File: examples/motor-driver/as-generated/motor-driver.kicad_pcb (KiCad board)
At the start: 2 copper layers, 100 x 50 mm, 12 parts, among them J1 VM 2.7-10.8V, J2 MOTOR A, J3 MOTOR B, J4 LOGIC, U1 DRV8833PW

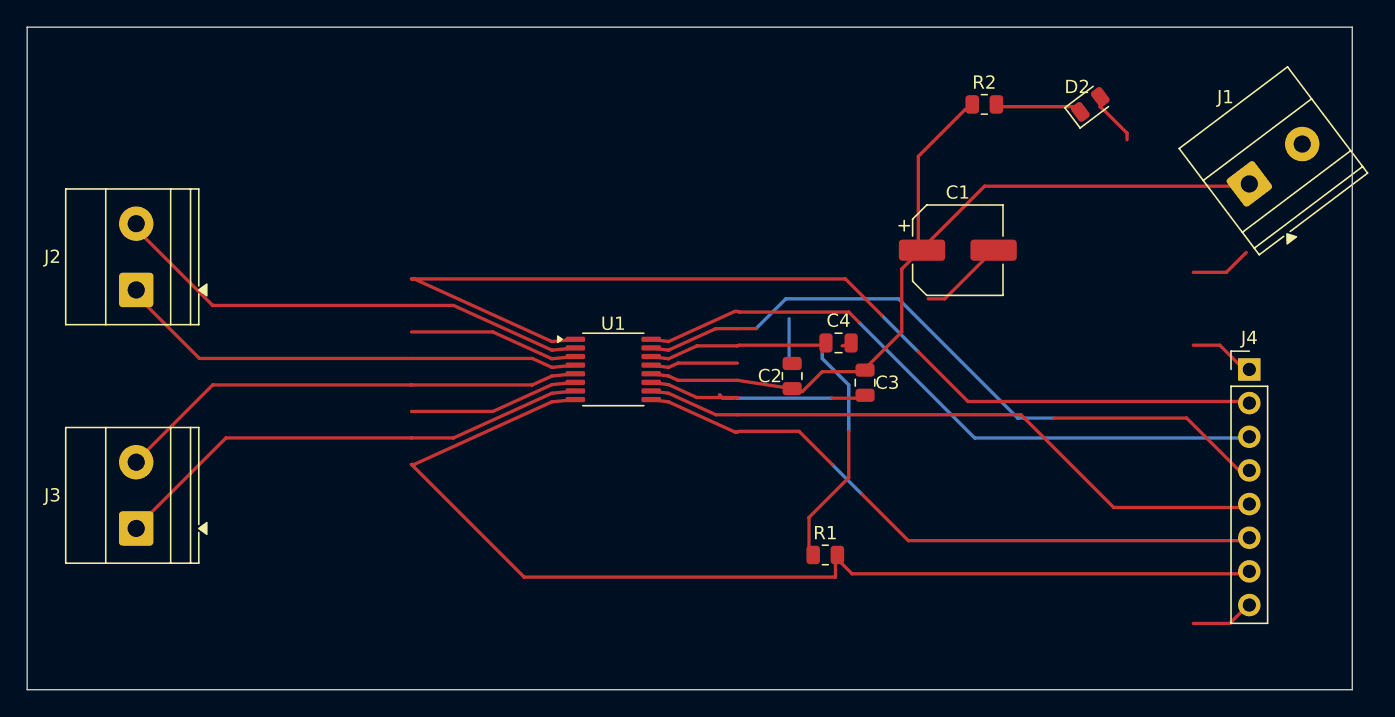
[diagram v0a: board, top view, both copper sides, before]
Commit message: Regenerate the five as round three drew them
All five reviewed projects pass their gates again: the buck all wire
with its feedback drawn home, the motor's logic named at the header,
the carrier reading as the pinout table it is - with its feed diode
finally pointing the right way - the filter compact with test points,
and the FPGA's capacitors sitting beside the units they feed. Thirty
renders redrawn, verdict tables at today's numbers.

Co-Authored-By: Claude Fable 5 <noreply@anthropic.com>
Claude-Session: https://claude.ai/code/session_01DUj7Ltu92tWg159mCSacwY
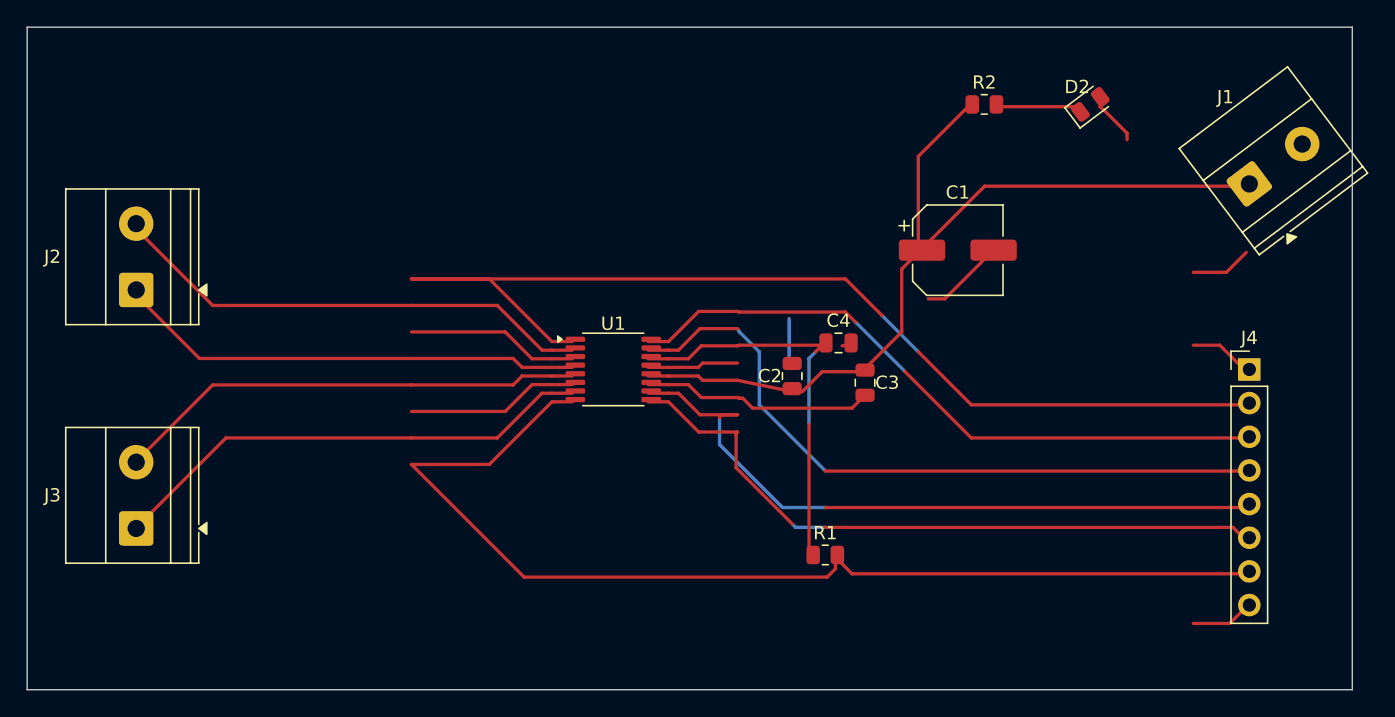
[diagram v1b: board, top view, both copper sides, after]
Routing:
- net /BIN2: track 48.2 -> 52.7 mm
- net /BIN1: track 48.8 -> 51.1 mm
- net /VCP: track 19.0 -> 17.2 mm
- net /VINT: track 31.3 -> 30.1 mm
- net /AIN2: track 51.6 -> 52.7 mm
- net /nSLEEP: track 80.4 -> 81.0 mm
- net /AIN1: track 49.4 -> 50.0 mm
- net GND: track 59.7 -> 60.3 mm

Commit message: Regenerate the four boards round four has settled
The buck, the motor driver, the carrier and the filter as the current
generator draws them: interior ground stitching on all four, the motor
driver's bundle tight and its board twelve millimetres shorter, the
filter compact and hand-placed, the carrier's indicator in a column of
its own. All four pass their gates. The FPGA is still regenerating.

Co-Authored-By: Claude Fable 5 <noreply@anthropic.com>
Claude-Session: https://claude.ai/code/session_01DUj7Ltu92tWg159mCSacwY
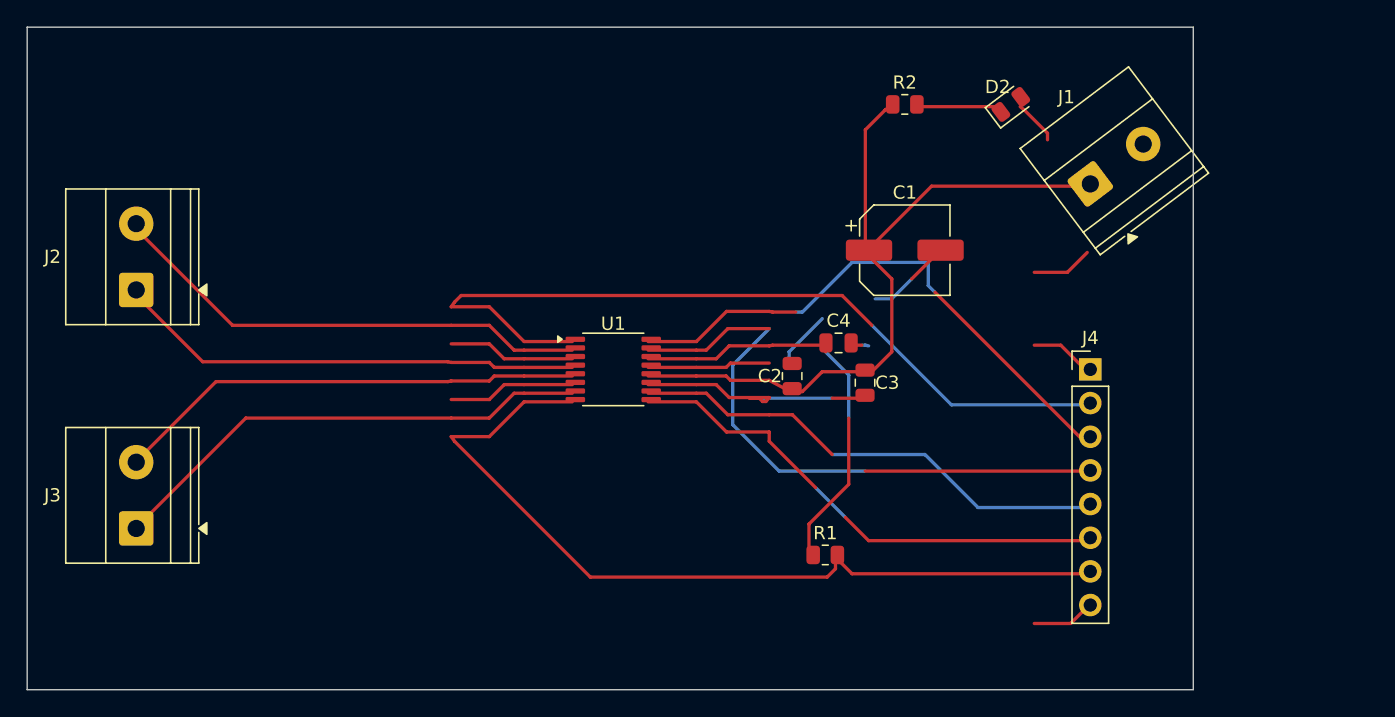
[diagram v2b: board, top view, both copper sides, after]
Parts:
- moved J1 12.0 mm to (180.2, 71.8)
- moved J4 12.0 mm to (180.2, 85.8)
- moved D2 6.00 mm to (174.2, 65.8)
- moved R2 6.00 mm to (166.2, 65.8)
- moved C1 4.00 mm to (166.2, 76.8)
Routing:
- net /nSLEEP: track 81.0 -> 62.0 mm
- net /nFAULT: track 82.3 -> 64.4 mm
- net /BIN2: track 52.7 -> 36.7 mm
- net /BIN1: track 51.1 -> 37.9 mm
- net /VM: track 67.2 -> 58.9 mm
- net /AIN1: track 50.0 -> 42.2 mm
- net /AIN2: track 52.7 -> 46.4 mm
- net /VCP: track 17.2 -> 19.8 mm
- net GND: track 60.3 -> 58.1 mm
- net /VINT: track 30.1 -> 31.7 mm
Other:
- board size 100 x 50 mm -> 88 x 50 mm

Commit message: Regenerate the four boards whose corners were off the grid
Ninety-one bends at angles nobody chose, now none. All four still pass
their gates.

Co-Authored-By: Claude Fable 5 <noreply@anthropic.com>
Claude-Session: https://claude.ai/code/session_01DUj7Ltu92tWg159mCSacwY
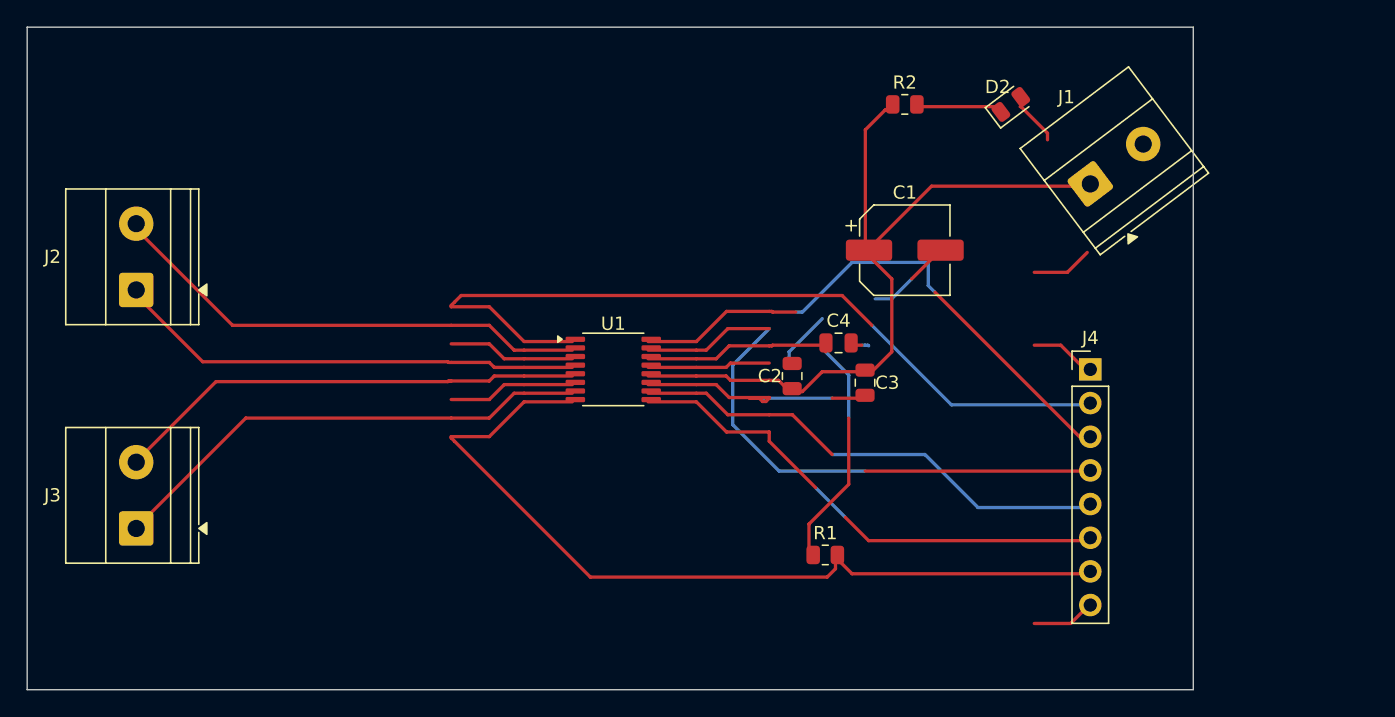
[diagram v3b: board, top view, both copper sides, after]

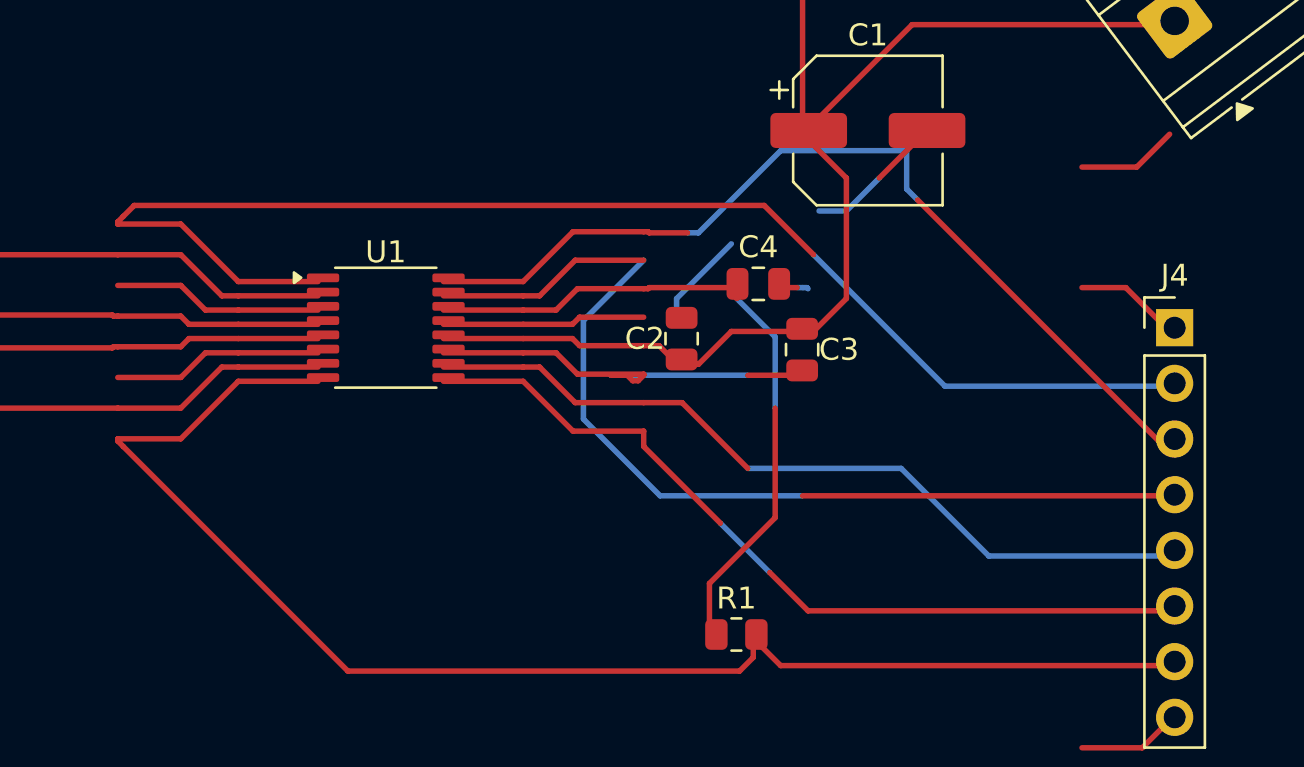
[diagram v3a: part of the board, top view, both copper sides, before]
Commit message: Regenerate the four the text and width work changed
Designators and values off the rails they were printed on, power-named
nets at the width their rule asks for, and the buck's feedback ending
on the capacitor pad it senses at.

Co-Authored-By: Claude Fable 5 <noreply@anthropic.com>
Claude-Session: https://claude.ai/code/session_01DUj7Ltu92tWg159mCSacwY
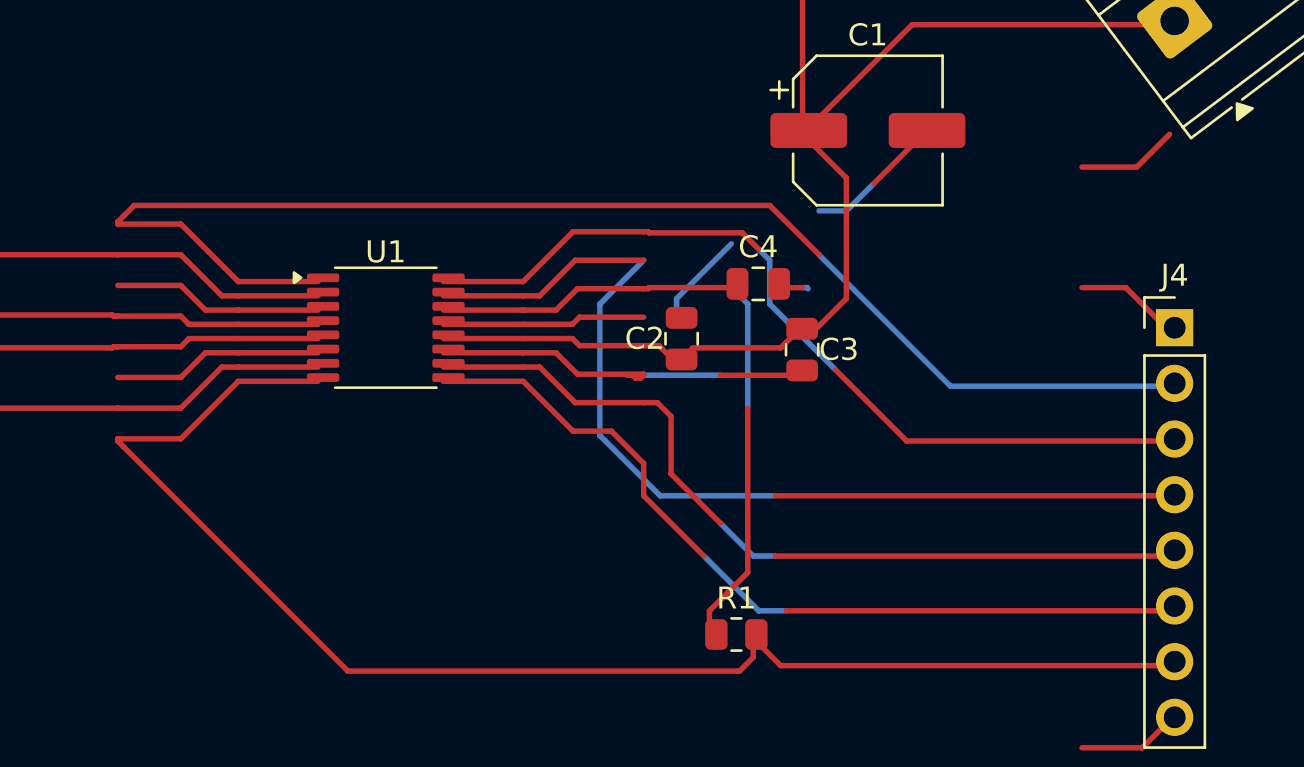
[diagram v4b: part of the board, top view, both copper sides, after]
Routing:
- net /AIN1: track 42.2 -> 39.2 mm
- net /VCP: track 19.8 -> 18.2 mm
- net /BIN2: track 36.7 -> 38.3 mm
- net /VINT: track 31.7 -> 30.7 mm
- net /AIN2: track 46.4 -> 45.8 mm
